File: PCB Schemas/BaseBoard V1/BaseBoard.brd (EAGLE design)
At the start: 94 x 31.1 mm, 31 parts, among them IC1 ATMEGA2560AU, J1 PROGRAM, U1 74HC595D, U2 74HC595D, U3 74HC595D, X1 16MHz

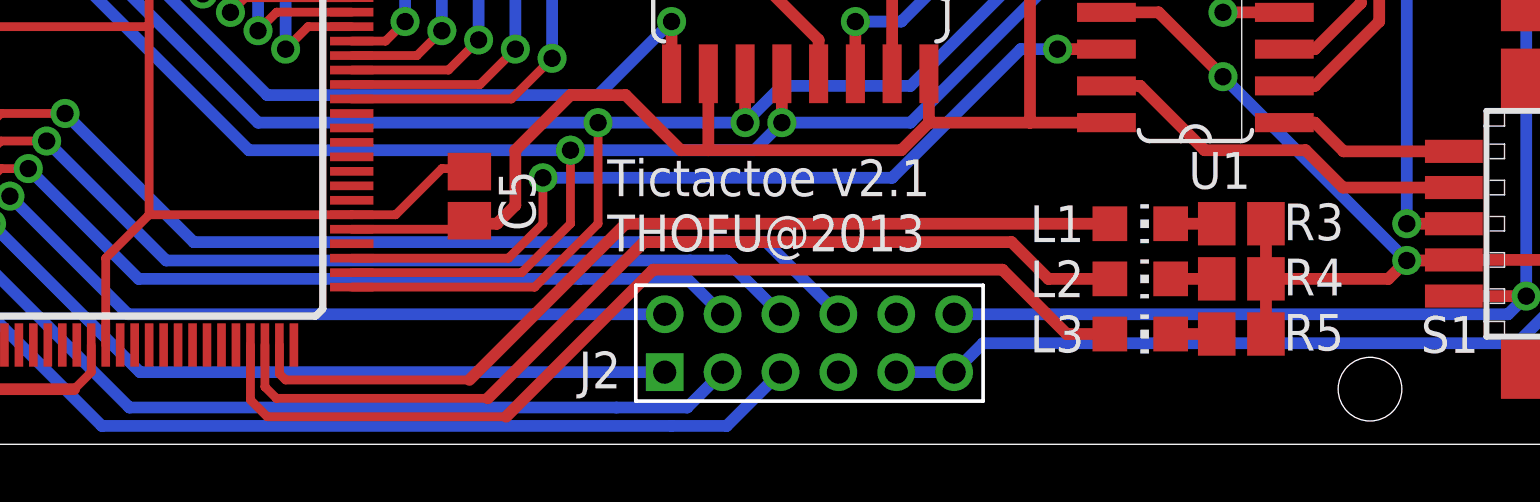
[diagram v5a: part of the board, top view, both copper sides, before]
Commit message: Revert "Changed debug pins"
This reverts commit 73787cc4df0c0002b7e389e6993c433356a097db.
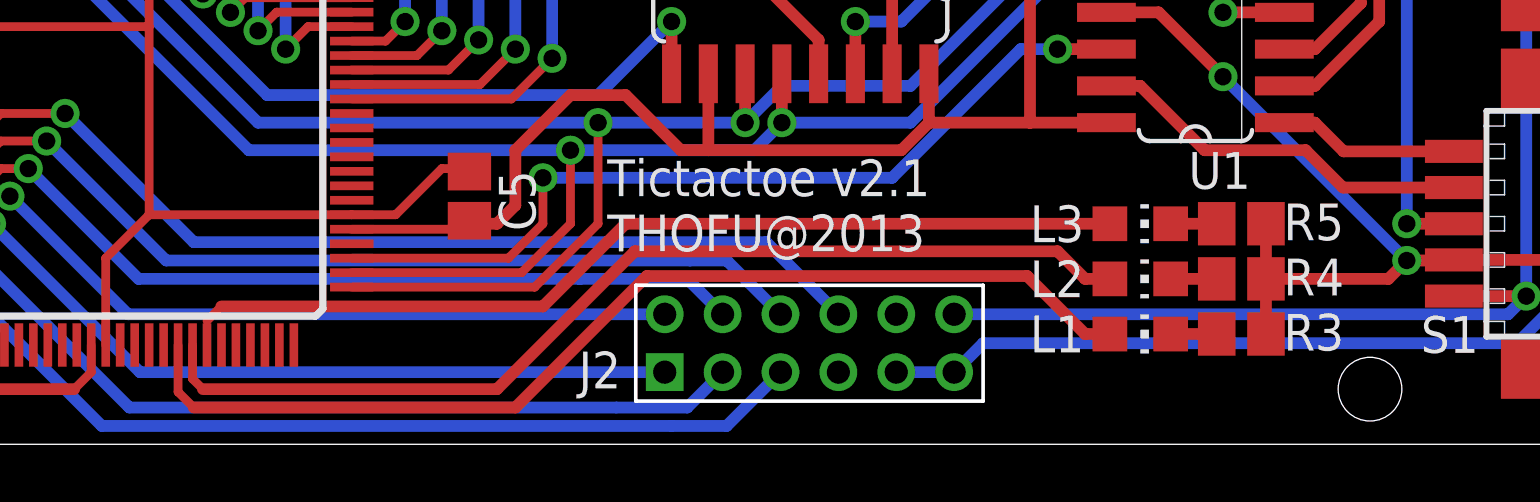
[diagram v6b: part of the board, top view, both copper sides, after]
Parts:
- moved L1 3.81 mm to (77.5, 3.81)
- moved L3 3.81 mm to (77.5, 7.62)
- moved R3 3.81 mm to (81.0, 3.81)
- moved R5 3.81 mm to (81.0, 7.62)
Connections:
- net DBG1: now also IC1.67; no longer IC1.74
- net DBG2: now also IC1.68; no longer IC1.73
- net DBG3: now also IC1.69; no longer IC1.72
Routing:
- net DBG1: track 32.0 -> 36.7 mm
- net DBG3: track 34.9 -> 32.6 mm
- net DBG2: track 33.6 -> 35.4 mm
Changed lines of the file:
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@@
 <attribute name="VALUE" x="27.178" y="1.524" size="1.27" layer="27"/>
 </element>
-<element name="R3" library="resistor" package="R0805" value="330" x="80.9625" y="7.62" smashed="yes">
+<element name="R3" library="resistor" package="R0805" value="330" x="80.9625" y="3.81" smashed="yes">
+<attribute name="NAME" x="82.423" y="3.2385" size="1.27" layer="25"/>
+<attribute name="VALUE" x="80.2005" y="1.524" size="1.27" layer="27"/>
+</element>
+<element name="ICSP" library="SparkFun-Connectors" package="2X3-NS" value="AVR_SPI_PRG_6NS" x="16.1925" y="5.3975" rot="R180"/>
+<element name="R5" library="resistor" package="R0805" value="330" x="80.9625" y="7.62" smashed="yes">
 <attribute name="NAME" x="82.423" y="7.0485" size="1.27" layer="25"/>
 <attribute name="VALUE" x="80.2005" y="5.334" size="1.27" layer="27"/>
-</element>
-<element name="ICSP" library="SparkFun-Connectors" package="2X3-NS" value="AVR_SPI_PRG_6NS" x="16.1925" y="5.3975" rot="R180"/>
-<element name="R5" library="resistor" package="R0805" value="330" x="80.9625" y="3.81" smashed="yes">
-<attribute name="NAME" x="82.423" y="3.2385" size="1.27" layer="25"/>
-<attribute name="VALUE" x="80.2005" y="1.524" size="1.27" layer="27"/>
 </element>
 <element name="R4" library="resistor" package="R0805" value="330" x="80.9625" y="5.715" smashed="yes">
@@
 <attribute name="VALUE" x="76.2" y="3.175" size="1.27" layer="27"/>
 </element>
-<element name="L3" library="led" package="CHIP-LED0805" value="" x="77.47" y="3.81" smashed="yes" rot="R270">
+<element name="L3" library="led" package="CHIP-LED0805" value="" x="77.47" y="7.62" smashed="yes" rot="R270">
+<attribute name="NAME" x="73.66" y="6.985" size="1.27" layer="25"/>
+<attribute name="VALUE" x="76.2" y="5.08" size="1.27" layer="27"/>
+</element>
+<element name="L1" library="led" package="CHIP-LED0805" value="" x="77.47" y="3.81" smashed="yes" rot="R270">
 <attribute name="NAME" x="73.66" y="3.175" size="1.27" layer="25"/>
 <attribute name="VALUE" x="76.2" y="1.27" size="1.27" layer="27"/>
-</element>
-<element name="L1" library="led" package="CHIP-LED0805" value="" x="77.47" y="7.62" smashed="yes" rot="R270">
-<attribute name="NAME" x="73.66" y="6.985" size="1.27" layer="25"/>
-<attribute name="VALUE" x="76.2" y="5.08" size="1.27" layer="27"/>
 </element>
 <element name="J2" library="Connectors" package="CON06X2_2MM" value="" x="66.04" y="3.4925" smashed="yes">
@@
 <wire x1="80.3275" y1="12.7" x2="86.6775" y2="6.35" width="0.4064" layer="16"/>
 <contactref element="R4" pad="2"/>
+<wire x1="81.8125" y1="3.81" x2="81.8125" y2="5.715" width="0.4064" layer="1"/>
 <wire x1="86.6775" y1="6.35" x2="86.0425" y2="5.715" width="0.4064" layer="1"/>
+<wire x1="86.0425" y1="5.715" x2="81.8125" y2="5.715" width="0.4064" layer="1"/>
 <wire x1="4.445" y1="16.8275" x2="4.445" y2="13.0175" width="0.4064" layer="16"/>
 <wire x1="4.445" y1="13.0175" x2="1.5875" y2="10.16" width="0.4064" layer="16"/>
@@
 <wire x1="90.4875" y1="3.4925" x2="72.04" y2="3.4925" width="0.4064" layer="16"/>
 <wire x1="72.04" y1="3.4925" x2="71.04" y2="2.4925" width="0.4064" layer="16"/>
-<wire x1="86.0425" y1="5.715" x2="81.8125" y2="5.715" width="0.4064" layer="1"/>
 <wire x1="81.8125" y1="7.62" x2="81.8125" y2="5.715" width="0.4064" layer="1"/>
-<wire x1="81.8125" y1="5.715" x2="81.8125" y2="3.81" width="0.4064" layer="1"/>
 </signal>
 <signal name="VCC">
@@
 <contactref element="R3" pad="1"/>
 <contactref element="L1" pad="C"/>
-<wire x1="78.52" y1="7.62" x2="80.1125" y2="7.62" width="0.4064" layer="1"/>
+<wire x1="78.52" y1="3.81" x2="80.1125" y2="3.81" width="0.4064" layer="1"/>
 </signal>
 <signal name="DBG2">
 <contactref element="L2" pad="A"/>
-<contactref element="IC1" pad="73"/>
-<wire x1="76.42" y1="5.715" x2="74.295" y2="5.715" width="0.4064" layer="1"/>
-<wire x1="74.295" y1="5.715" x2="73.025" y2="6.985" width="0.4064" layer="1"/>
-<wire x1="73.025" y1="6.985" x2="60.325" y2="6.985" width="0.4064" layer="1"/>
-<wire x1="60.325" y1="6.985" x2="54.9275" y2="1.5875" width="0.4064" layer="1"/>
-<wire x1="47.2275" y1="3.43" x2="47.2275" y2="1.985" width="0.3048" layer="1"/>
-<wire x1="47.2275" y1="1.985" x2="47.625" y2="1.5875" width="0.3048" layer="1"/>
-<wire x1="47.625" y1="1.5875" x2="54.9275" y2="1.5875" width="0.3048" layer="1"/>
+<contactref element="IC1" pad="68"/>
+<wire x1="44.7275" y1="3.43" x2="44.7275" y2="2.2625" width="0.3048" layer="1"/>
+<wire x1="44.7275" y1="2.2625" x2="45.085" y2="1.905" width="0.3048" layer="1"/>
+<wire x1="60.0075" y1="6.6675" x2="55.245" y2="1.905" width="0.4064" layer="1"/>
+<wire x1="55.245" y1="1.905" x2="45.085" y2="1.905" width="0.4064" layer="1"/>
+<wire x1="60.0075" y1="6.6675" x2="74.6125" y2="6.6675" width="0.4064" layer="1"/>
+<wire x1="74.6125" y1="6.6675" x2="75.565" y2="5.715" width="0.4064" layer="1"/>
+<wire x1="75.565" y1="5.715" x2="76.42" y2="5.715" width="0.4064" layer="1"/>
 </signal>
 <signal name="DBG3">
 <contactref element="L3" pad="A"/>
-<contactref element="IC1" pad="72"/>
-<wire x1="76.42" y1="3.81" x2="74.93" y2="3.81" width="0.4064" layer="1"/>
-<wire x1="74.93" y1="3.81" x2="72.7075" y2="6.0325" width="0.4064" layer="1"/>
-<wire x1="72.7075" y1="6.0325" x2="60.6425" y2="6.0325" width="0.4064" layer="1"/>
-<wire x1="60.6425" y1="6.0325" x2="55.5625" y2="0.9525" width="0.4064" layer="1"/>
-<wire x1="46.7275" y1="3.43" x2="46.7275" y2="1.5325" width="0.3048" layer="1"/>
-<wire x1="46.7275" y1="1.5325" x2="47.3075" y2="0.9525" width="0.3048" layer="1"/>
-<wire x1="47.3075" y1="0.9525" x2="55.5625" y2="0.9525" width="0.3048" layer="1"/>
+<wire x1="59.69" y1="7.62" x2="76.42" y2="7.62" width="0.4064" layer="1"/>
+<wire x1="45.2275" y1="4.27" x2="45.72" y2="4.7625" width="0.3048" layer="1"/>
+<wire x1="45.72" y1="4.7625" x2="56.8325" y2="4.7625" width="0.4064" layer="1"/>
+<wire x1="56.8325" y1="4.7625" x2="59.69" y2="7.62" width="0.4064" layer="1"/>
+<contactref element="IC1" pad="69"/>
+<wire x1="45.2275" y1="3.43" x2="45.2275" y2="4.27" width="0" layer="19" extent="1-1"/>
 </signal>
 <signal name="RED4">
@@
 <signal name="DBG1">
 <contactref element="L1" pad="A"/>
-<contactref element="IC1" pad="74"/>
-<wire x1="76.42" y1="7.62" x2="59.69" y2="7.62" width="0.4064" layer="1"/>
-<wire x1="59.69" y1="7.62" x2="54.2925" y2="2.2225" width="0.4064" layer="1"/>
-<wire x1="47.7275" y1="3.43" x2="47.7275" y2="2.4375" width="0.3048" layer="1"/>
-<wire x1="47.7275" y1="2.4375" x2="47.9425" y2="2.2225" width="0.3048" layer="1"/>
-<wire x1="47.9425" y1="2.2225" x2="54.2925" y2="2.2225" width="0.3048" layer="1"/>
+<contactref element="IC1" pad="67"/>
+<wire x1="44.2275" y1="3.43" x2="44.2275" y2="1.81" width="0.3048" layer="1"/>
+<wire x1="44.2275" y1="1.81" x2="44.7675" y2="1.27" width="0.3048" layer="1"/>
+<wire x1="60.4225" y1="5.8125" x2="55.88" y2="1.27" width="0.4064" layer="1"/>
+<wire x1="55.88" y1="1.27" x2="44.7675" y2="1.27" width="0.4064" layer="1"/>
+<wire x1="60.4225" y1="5.8125" x2="73.5625" y2="5.8125" width="0.4064" layer="1"/>
+<wire x1="73.5625" y1="5.8125" x2="75.565" y2="3.81" width="0.4064" layer="1"/>
+<wire x1="75.565" y1="3.81" x2="76.42" y2="3.81" width="0.4064" layer="1"/>
 </signal>
 <signal name="N$3">
@@
 <contactref element="R5" pad="1"/>
 <contactref element="L3" pad="C"/>
-<wire x1="78.52" y1="3.81" x2="80.1125" y2="3.81" width="0.4064" layer="1"/>
+<wire x1="78.52" y1="7.62" x2="80.1125" y2="7.62" width="0.4064" layer="1"/>
 </signal>
 <signal name="+3.3V">

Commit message: Revised PCB schemas
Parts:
- moved L1 3.81 mm to (77.5, 7.62)
- moved L3 3.81 mm to (77.5, 3.81)
- moved R3 3.81 mm to (81.0, 7.62)
- moved R5 3.81 mm to (81.0, 3.81)
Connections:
- net +3.3V: now also J2.5; no longer J2.10
- net +VIN: now also J2.9; no longer J2.7
- net BASE_RX: now also IC1.46, J2.3; no longer IC1.45, J2.1
- net BASE_TX: now also IC1.45, J2.1; no longer IC1.46, J2.3
- net DBG1: now also L3.A; no longer L1.A
- net DBG3: now also L1.A; no longer L3.A
- net GND: now also J2.12; no longer J2.9
- net INT_EXT: now also IC1.40, J2.10; no longer IC1.47, J2.5
- net VCC: now also J2.7; no longer J2.12
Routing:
- net GND: track 380.4 -> 368.8 mm
- net VCC: track 318.6 -> 324.6 mm
- net INT_EXT: track 34.2 -> 38.9 mm
- net BASE_TX: track 31.9 -> 29.1 mm
- net BASE_RX: track 29.1 -> 31.9 mm
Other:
- board text added: "Tictactoe v1.1 THOFU@2013"
- board text removed: "Tictactoe v2.1 THOFU@2013"
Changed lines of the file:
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@@
 <?xml version="1.0" encoding="utf-8"?>
 <!DOCTYPE eagle SYSTEM "eagle.dtd">
-<eagle version="6.5.0">
+<eagle version="6.6.0">
 <drawing>
 <settings>
@@
 <setting verticaltext="up"/>
 </settings>
-<grid distance="0.0125" unitdist="inch" unit="inch" style="lines" multiple="1" display="no" altdistance="0.025" altunitdist="inch" altunit="inch"/>
+<grid distance="0.0125" unitdist="inch" unit="mm" style="lines" multiple="1" display="no" altdistance="0.025" altunitdist="inch" altunit="inch"/>
 <layers>
 <layer number="1" name="Top" color="4" fill="1" visible="yes" active="yes"/>
@@
 <wire x1="93.98" y1="31.115" x2="0" y2="31.115" width="0" layer="20"/>
 <wire x1="0" y1="31.115" x2="0" y2="0" width="0" layer="20"/>
-<hole x="92.075" y="29.21" drill="2.2"/>
-<hole x="1.905" y="19.05" drill="2.2"/>
-<hole x="85.4075" y="1.905" drill="2.2"/>
-<text x="59.055" y="6.6675" size="1.27" layer="25">Tictactoe v2.1
+<hole x="92.075" y="29.21" drill="2.6"/>
+<hole x="1.905" y="19.05" drill="2.6"/>
+<hole x="85.4075" y="1.905" drill="2.6"/>
+<text x="59.055" y="6.6675" size="1.27" layer="25">Tictactoe v1.1
 THOFU@2013</text>
 <text x="4.445" y="3.175" size="1.016" layer="25" rot="R270">gnd</text>
@@
 <attribute name="VALUE" x="27.178" y="1.524" size="1.27" layer="27"/>
 </element>
-<element name="R3" library="resistor" package="R0805" value="330" x="80.9625" y="3.81" smashed="yes">
+<element name="R5" library="resistor" package="R0805" value="330" x="80.9625" y="3.81" smashed="yes">
 <attribute name="NAME" x="82.423" y="3.2385" size="1.27" layer="25"/>
 <attribute name="VALUE" x="80.2005" y="1.524" size="1.27" layer="27"/>
 </element>
 <element name="ICSP" library="SparkFun-Connectors" package="2X3-NS" value="AVR_SPI_PRG_6NS" x="16.1925" y="5.3975" rot="R180"/>
-<element name="R5" library="resistor" package="R0805" value="330" x="80.9625" y="7.62" smashed="yes">
+<element name="R3" library="resistor" package="R0805" value="330" x="80.9625" y="7.62" smashed="yes">
 <attribute name="NAME" x="82.423" y="7.0485" size="1.27" layer="25"/>
 <attribute name="VALUE" x="80.2005" y="5.334" size="1.27" layer="27"/>
@@
 <attribute name="VALUE" x="76.2" y="3.175" size="1.27" layer="27"/>
 </element>
-<element name="L3" library="led" package="CHIP-LED0805" value="" x="77.47" y="7.62" smashed="yes" rot="R270">
+<element name="L1" library="led" package="CHIP-LED0805" value="" x="77.47" y="7.62" smashed="yes" rot="R270">
 <attribute name="NAME" x="73.66" y="6.985" size="1.27" layer="25"/>
 <attribute name="VALUE" x="76.2" y="5.08" size="1.27" layer="27"/>
 </element>
-<element name="L1" library="led" package="CHIP-LED0805" value="" x="77.47" y="3.81" smashed="yes" rot="R270">
+<element name="L3" library="led" package="CHIP-LED0805" value="" x="77.47" y="3.81" smashed="yes" rot="R270">
 <attribute name="NAME" x="73.66" y="3.175" size="1.27" layer="25"/>
 <attribute name="VALUE" x="76.2" y="1.27" size="1.27" layer="27"/>
@@
 <contactref element="U2" pad="13"/>
 <contactref element="R2" pad="2"/>
-<contactref element="R3" pad="2"/>
+<contactref element="R5" pad="2"/>
 <contactref element="S9" pad="2"/>
 <contactref element="S4" pad="2"/>
@@
 <wire x1="4.445" y1="13.0175" x2="1.5875" y2="10.16" width="0.4064" layer="16"/>
 <wire x1="1.5875" y1="10.16" x2="1.5875" y2="3.4925" width="0.4064" layer="16"/>
-<wire x1="90.4875" y1="3.4925" x2="92.075" y2="5.08" width="0.4064" layer="16"/>
-<wire x1="92.075" y1="5.08" x2="92.075" y2="6.37" width="0.4064" layer="16"/>
 <wire x1="22.5425" y1="14.39" x2="22.5425" y2="14.2875" width="0.4064" layer="1"/>
 <wire x1="22.5425" y1="11.645" x2="22.5425" y2="14.2875" width="0.4064" layer="1"/>
@@
 <wire x1="28.8925" y1="2.54" x2="28.8925" y2="3.7075" width="0.4064" layer="1"/>
 <wire x1="28.8925" y1="3.7075" x2="28.79" y2="3.81" width="0.4064" layer="1"/>
-<contactref element="R5" pad="2"/>
+<contactref element="R3" pad="2"/>
+<wire x1="81.8125" y1="7.62" x2="81.8125" y2="5.715" width="0.4064" layer="1"/>
+<wire x1="81.8125" y1="3.81" x2="81.8125" y2="3.0725" width="0.4064" layer="1"/>
 <contactref element="J2" pad="11"/>
-<contactref element="J2" pad="9"/>
-<wire x1="69.04" y1="2.4925" x2="71.04" y2="2.4925" width="0.4064" layer="16"/>
-<wire x1="90.4875" y1="3.4925" x2="72.04" y2="3.4925" width="0.4064" layer="16"/>
-<wire x1="72.04" y1="3.4925" x2="71.04" y2="2.4925" width="0.4064" layer="16"/>
-<wire x1="81.8125" y1="7.62" x2="81.8125" y2="5.715" width="0.4064" layer="1"/>
+<contactref element="J2" pad="12"/>
+<wire x1="71.04" y1="4.4925" x2="71.04" y2="2.4925" width="0.4064" layer="1"/>
+<wire x1="81.8125" y1="3.0725" x2="81.2325" y2="2.4925" width="0.4064" layer="1"/>
+<wire x1="81.2325" y1="2.4925" x2="71.04" y2="2.4925" width="0.4064" layer="1"/>
 </signal>
 <signal name="VCC">
@@
 <wire x1="7.405" y1="10.0575" x2="5.715" y2="11.7475" width="0.4064" layer="1"/>
 <wire x1="9.525" y1="10.16" x2="7.405" y2="10.16" width="0.4064" layer="1"/>
-<contactref element="J2" pad="12"/>
-<wire x1="71.04" y1="4.4925" x2="90.1775" y2="4.4925" width="0.4064" layer="16"/>
-<wire x1="90.1775" y1="4.4925" x2="90.805" y2="5.12" width="0.4064" layer="16"/>
+<contactref element="J2" pad="7"/>
+<wire x1="67.04" y1="2.4925" x2="68.2625" y2="1.27" width="0.4064" layer="16"/>
+<wire x1="68.2625" y1="1.27" x2="73.66" y2="1.27" width="0.4064" layer="16"/>
+<wire x1="73.66" y1="1.27" x2="76.5175" y2="4.1275" width="0.4064" layer="16"/>
+<wire x1="76.5175" y1="4.1275" x2="90.17" y2="4.1275" width="0.4064" layer="16"/>
+<wire x1="90.17" y1="4.1275" x2="90.805" y2="4.7625" width="0.4064" layer="16"/>
+<wire x1="90.805" y1="4.7625" x2="90.805" y2="5.12" width="0.4064" layer="16"/>
 </signal>
 <signal name="RESET">
@@
 </signal>
 <signal name="N$9">
-<contactref element="R3" pad="1"/>
-<contactref element="L1" pad="C"/>
+<contactref element="R5" pad="1"/>
+<contactref element="L3" pad="C"/>
 <wire x1="78.52" y1="3.81" x2="80.1125" y2="3.81" width="0.4064" layer="1"/>
 </signal>
@@
 </signal>
 <signal name="DBG3">
-<contactref element="L3" pad="A"/>
+<contactref element="L1" pad="A"/>
 <wire x1="59.69" y1="7.62" x2="76.42" y2="7.62" width="0.4064" layer="1"/>
 <wire x1="45.2275" y1="4.27" x2="45.72" y2="4.7625" width="0.3048" layer="1"/>
@@
 </signal>
 <signal name="BASE_TX">
-<contactref element="IC1" pad="46"/>
-<via x="37.1475" y="6.6675" extent="1-16" drill="0.6"/>
-<wire x1="37.1475" y1="6.6675" x2="42.545" y2="1.27" width="0.4064" layer="16"/>
-<wire x1="42.545" y1="1.27" x2="59.3725" y2="1.27" width="0.4064" layer="16"/>
-<wire x1="34.2275" y1="7.43" x2="36.385" y2="7.43" width="0.3048" layer="1"/>
-<wire x1="36.385" y1="7.43" x2="37.1475" y2="6.6675" width="0.3048" layer="1"/>
-<contactref element="J2" pad="3"/>
-<wire x1="63.04" y1="2.4925" x2="61.8175" y2="1.27" width="0.4064" layer="16"/>
-<wire x1="61.8175" y1="1.27" x2="59.3725" y2="1.27" width="0.4064" layer="16"/>
-</signal>
-<signal name="BASE_RX">
 <contactref element="IC1" pad="45"/>
 <via x="37.7825" y="7.62" extent="1-16" drill="0.6"/>
@@
 </signal>
 <signal name="INT_EXT">
-<contactref element="IC1" pad="47"/>
-<wire x1="61.2775" y1="0.635" x2="41.5925" y2="0.635" width="0.4064" layer="16"/>
-<wire x1="41.5925" y1="0.635" x2="36.5125" y2="5.715" width="0.4064" layer="16"/>
-<via x="36.5125" y="5.715" extent="1-16" drill="0.6"/>
-<wire x1="34.2275" y1="6.93" x2="35.2975" y2="6.93" width="0.3048" layer="1"/>
-<wire x1="35.2975" y1="6.93" x2="36.5125" y2="5.715" width="0.3048" layer="1"/>
-<contactref element="J2" pad="5"/>
-<wire x1="65.04" y1="2.4925" x2="63.1825" y2="0.635" width="0.4064" layer="16"/>
-<wire x1="63.1825" y1="0.635" x2="61.2775" y2="0.635" width="0.4064" layer="16"/>
+<contactref element="J2" pad="10"/>
+<contactref element="IC1" pad="40"/>
+<wire x1="34.2275" y1="10.43" x2="36.1475" y2="10.43" width="0.3048" layer="1"/>
+<wire x1="36.1475" y1="10.43" x2="38.1" y2="12.3825" width="0.3048" layer="1"/>
+<wire x1="38.1" y1="12.3825" x2="41.275" y2="12.3825" width="0.3048" layer="1"/>
+<via x="41.275" y="12.3825" extent="1-16" drill="0.6"/>
+<wire x1="41.275" y1="12.3825" x2="45.72" y2="7.9375" width="0.4064" layer="16"/>
+<wire x1="45.72" y1="7.9375" x2="65.595" y2="7.9375" width="0.4064" layer="16"/>
+<wire x1="65.595" y1="7.9375" x2="69.04" y2="4.4925" width="0.4064" layer="16"/>
 </signal>
 <signal name="DBG1">
-<contactref element="L1" pad="A"/>
+<contactref element="L3" pad="A"/>
 <contactref element="IC1" pad="67"/>
 <wire x1="44.2275" y1="3.43" x2="44.2275" y2="1.81" width="0.3048" layer="1"/>
@@
 </signal>
 <signal name="N$4">
-<contactref element="R5" pad="1"/>
-<contactref element="L3" pad="C"/>
+<contactref element="R3" pad="1"/>
+<contactref element="L1" pad="C"/>
 <wire x1="78.52" y1="7.62" x2="80.1125" y2="7.62" width="0.4064" layer="1"/>
 </signal>
+<signal name="+VIN">
+<contactref element="J2" pad="9"/>
+</signal>
+<signal name="BASE_RX">
+<contactref element="IC1" pad="46"/>
+<via x="37.1475" y="6.6675" extent="1-16" drill="0.6"/>
+<wire x1="37.1475" y1="6.6675" x2="42.545" y2="1.27" width="0.4064" layer="16"/>
+<wire x1="42.545" y1="1.27" x2="59.3725" y2="1.27" width="0.4064" layer="16"/>
+<wire x1="36.385" y1="7.43" x2="37.1475" y2="6.6675" width="0.3048" layer="1"/>
+<contactref element="J2" pad="3"/>
+<wire x1="63.04" y1="2.4925" x2="61.8175" y2="1.27" width="0.4064" layer="16"/>
+<wire x1="61.8175" y1="1.27" x2="59.3725" y2="1.27" width="0.4064" layer="16"/>
+<wire x1="34.2275" y1="7.43" x2="36.385" y2="7.43" width="0.3048" layer="1"/>
+</signal>
 <signal name="+3.3V">
-<contactref element="J2" pad="10"/>
-</signal>
-<signal name="+VIN">
-<contactref element="J2" pad="7"/>
+<contactref element="J2" pad="5"/>
 </signal>
 </signals>
